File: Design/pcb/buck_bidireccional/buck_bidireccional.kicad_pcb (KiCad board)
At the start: 2 copper layers, 85 x 60 mm, 27 parts, among them J2 Screw_Terminal_01x02, J3 Screw_Terminal_01x02, Q1 NMOS, Q2 NMOS, U1 IR2184

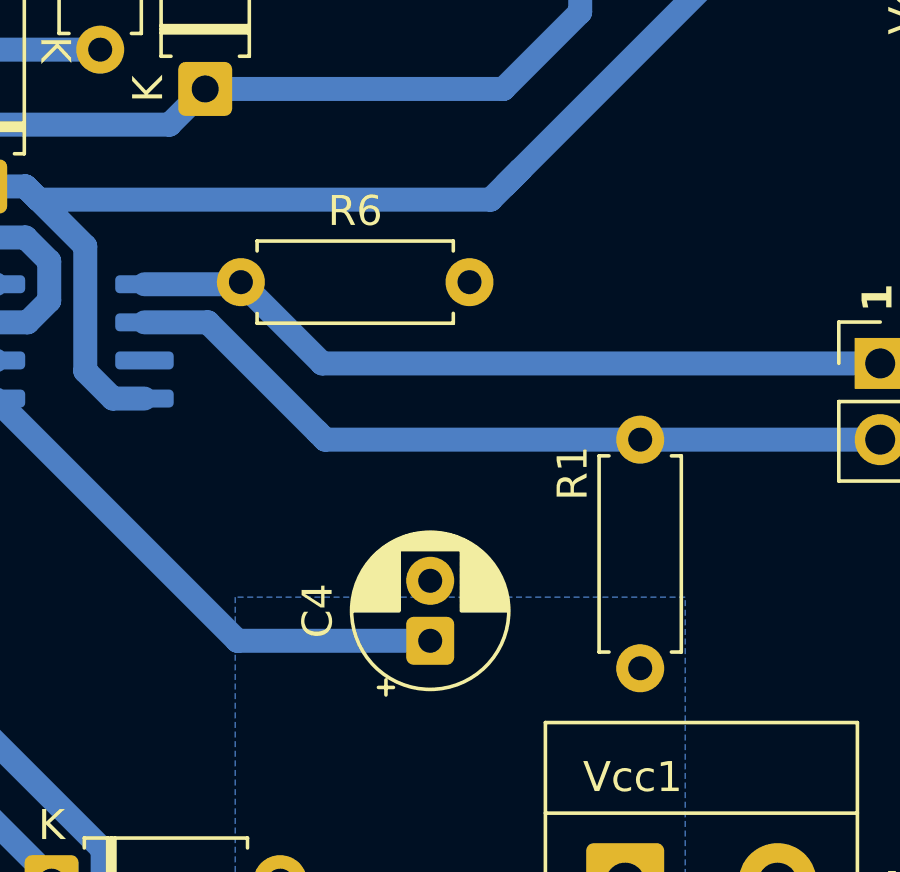
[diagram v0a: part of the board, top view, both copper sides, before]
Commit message: removed non needed resistors
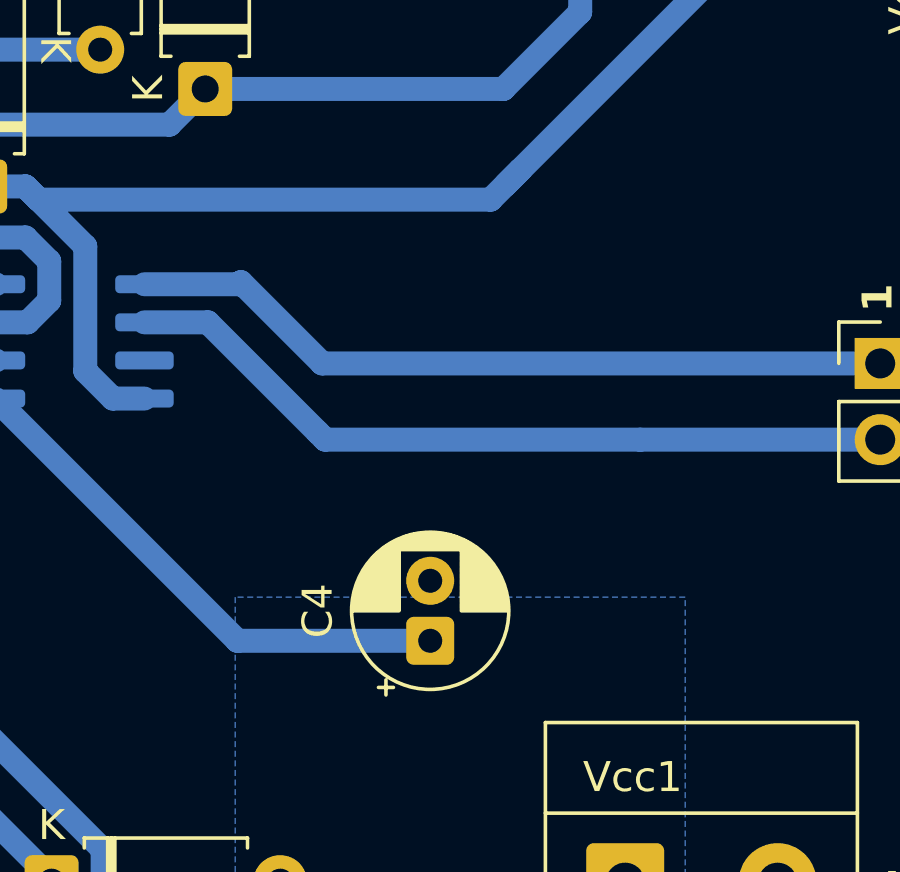
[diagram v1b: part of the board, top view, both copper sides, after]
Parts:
- removed R1, R6: 10k, Resistor_THT:R_Axial_DIN0207_L6.3mm_D2.5mm_P7.62mm_Horizontal

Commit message: fixed ids
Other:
- board text added: "DQ1"
- board text removed: "SQ1"
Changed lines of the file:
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@@
 		)
 	)
-	(gr_text "SQ1\n"
+	(gr_text "DQ1\n"
 		(at 110.5 102.5 90)
 		(layer "F.SilkS")

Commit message: a lot of stuff
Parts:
- moved PWM1 2.72 mm to (177.2, 108.5)
- moved R5 1.31 mm to (161.2, 97.4)
- moved D2 1.25 mm to (154.5, 100.8)
- moved R2 1.00 mm to (174.8, 91.5)
- moved Vgs_Q2 1.00 mm to (180.0, 95.8)
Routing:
- net LO: track 63.7 -> 0.44 mm
- net HO: track 42.0 -> 0.07 mm
- net Net-(D3-K): track 46.9 -> 11.5 mm
- net Net-(PWM1-Pin_2): track 26.1 -> 0.00 mm
- net Net-(PWM1-Pin_1): track 25.7 -> 0.00 mm
- net Net-(D4-K): track 24.2 -> 0.00 mm
- net Net-(D2-K): track 44.2 -> 21.5 mm
- net +12V: track 17.8 -> 0.00 mm
- net VS: track 58.5 -> 42.1 mm
- added copper zone on B.Cu, net HO
- added copper zone on B.Cu, net LO
- added copper zone on B.Cu, net Net-(D2-K)
- added copper zone on B.Cu, net Net-(D3-K)
- added copper zone on B.Cu, net Net-(D4-K)
- added copper zone on B.Cu, net Net-(PWM1-Pin_1)
- added copper zone on B.Cu, net Net-(PWM1-Pin_2)
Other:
- board text added: "SQ1"
- board text removed: "1"
- board text removed: "DQ1"

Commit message: updated pcb
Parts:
- moved D4 4.91 mm to (144.5, 128.0)
- moved PWM1 2.75 mm to (174.5, 108.5)
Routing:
- net VS: track 42.1 -> 0.00 mm
- net Net-(D3-K): track 11.5 -> 0.00 mm
- net Net-(D2-K): track 21.5 -> 20.1 mm
